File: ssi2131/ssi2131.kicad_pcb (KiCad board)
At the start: 2 copper layers, 40.2 x 108 mm, 34 parts, among them J1 Saw Out, J2 Pulse Out, J3 Tri Out, J4 Hard Sync, J5 Soft Sync, J6 Expo Freq, J7 16-Pin uZeus Power Header, U1 SSI2131, U2 LM4040DBZ-2.5

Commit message: PCB attempt 1
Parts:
- removed J6: Expo Freq, Connector_Audio:Jack_3.5mm_QingPu_WQP-PJ398SM_Vertical_CircularHoles
- added J9: Expo Freq, Connector_Audio:Jack_3.5mm_QingPu_WQP-PJ398SM_Vertical_CircularHoles, F.Cu at (135.3, 55.9)
- C1, C2, C3, C4, C5, C6, C7: footprint Capacitor_THT:C_Disc_D9.0mm_W2.5mm_P5.00mm -> Capacitor_THT:C_Disc_D6.0mm_W2.5mm_P5.00mm
- J7: footprint Connector_PinHeader_2.54mm:PinHeader_2x08_P2.54mm_Horizontal -> Connector_PinHeader_2.54mm:PinHeader_2x08_P2.54mm_Vertical; moved to B.Cu
- R1, R10, R13, R16, R2, R3, R4, R5, R6, R7, R9: footprint Resistor_THT:R_Axial_DIN0207_L6.3mm_D2.5mm_P10.16mm_Horizontal -> Resistor_THT:R_Axial_DIN0207_L6.3mm_D2.5mm_P2.54mm_Vertical
- R11: value 100 kOhms -> 220 kOhms; footprint Resistor_THT:R_Axial_DIN0207_L6.3mm_D2.5mm_P10.16mm_Horizontal -> Resistor_THT:R_Axial_DIN0207_L6.3mm_D2.5mm_P2.54mm_Vertical
- R12: value 100 kOhms -> 47 kOhms; footprint Resistor_THT:R_Axial_DIN0207_L6.3mm_D2.5mm_P10.16mm_Horizontal -> Resistor_THT:R_Axial_DIN0207_L6.3mm_D2.5mm_P2.54mm_Vertical
- R14: value 220 kOhms -> 100 kOhms; footprint Resistor_THT:R_Axial_DIN0207_L6.3mm_D2.5mm_P10.16mm_Horizontal -> Resistor_THT:R_Axial_DIN0207_L6.3mm_D2.5mm_P2.54mm_Vertical
- R15: value 47 kOhms -> 100 kOhms; footprint Resistor_THT:R_Axial_DIN0207_L6.3mm_D2.5mm_P10.16mm_Horizontal -> Resistor_THT:R_Axial_DIN0207_L6.3mm_D2.5mm_P2.54mm_Vertical
- RV2: value Expo Scale Knob - 5 kOhms -> Expo Scale Trim - 5 kOhms; moved to B.Cu
- moved C1 138.3 mm to (112.9, 38.1)
- moved C6 123.0 mm to (106.7, 58.4), turned to 180 degrees
- moved C2 119.8 mm to (114.3, 48.3), turned to 180 degrees
- moved C4 112.0 mm to (96.5, 81.3), turned to 180 degrees
- moved U2 111.4 mm to (94.0, 104.1), turned to -90 degrees
- moved C3 104.3 mm to (111.8, 121.9), turned to 90 degrees
- moved C7 97.4 mm to (116.8, 76.2), turned to 180 degrees
- moved C5 92.2 mm to (116.8, 81.3), turned to 180 degrees
- moved R8 89.1 mm to (101.6, 109.2), turned to 90 degrees
- moved R10 84.1 mm to (101.6, 94.0)
- moved U1 83.9 mm to (114.3, 94.0), turned to 180 degrees
- moved R1 82.0 mm to (94.0, 86.4)
- moved R4 81.9 mm to (123.1, 38.1), turned to 180 degrees
- moved R3 80.5 mm to (94.0, 96.5)
- moved R2 77.1 mm to (94.0, 91.4)
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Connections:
- net +2V5 renamed VREF
- net Net-(C1-Pad2) renamed HardSync
- net Net-(C2-Pad1) renamed SoftSync
- net Net-(C5-Pad1) renamed TCAP
- net Net-(J1-PadT) renamed SawOut
- net Net-(J2-PadT) renamed PulseOut
- net Net-(J3-PadT) renamed TriOut
- net Net-(R10-Pad2) renamed LinFreq
- net Net-(R5-Pad1) renamed BWComp
- net Net-(RV1-Pad2) renamed PWMCtrl
- net Net-(RV2-Pad1) renamed ExpoScale
- J7 pad 11: unconnected-(J7-Pad11) -> +5V
- J7 pad 12: unconnected-(J7-Pad12) -> +5V
- J7 pad 2: unconnected-(J7-Pad2) -> -12V
- J7 pad 4: unconnected-(J7-Pad4) -> GND
- J7 pad 6: unconnected-(J7-Pad6) -> GND
- J7 pad 8: unconnected-(J7-Pad8) -> GND
- J7 pad 9: +5V -> unconnected-(J7-Pad9)
- R11 pad 1: Net-(J6-PadT) -> Net-(R11-Pad1)
- R11 pad 2: Net-(R11-Pad2) -> ExpoFreq
- R12 pad 1: Net-(J6-PadT) -> HFTrack
- R12 pad 2: Net-(R11-Pad2) -> Net-(R11-Pad1)
- R14 pad 1: Net-(R11-Pad2) -> Net-(J9-PadT)
- R14 pad 2: Net-(R14-Pad2) -> ExpoFreq
- R15 pad 1: Net-(R14-Pad2) -> Net-(J9-PadT)
- R15 pad 2: Net-(R15-Pad2) -> ExpoFreq
- R6 pad 1: Net-(R15-Pad2) -> HFTrack
- R7 pad 1: Net-(R15-Pad2) -> HFTrack
- U1 pad 5: Net-(R15-Pad2) -> HFTrack
- U1 pad 6: Net-(R11-Pad2) -> ExpoFreq
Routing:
- net VREF: track 0.00 -> 193.2 mm
- net -12V: track 0.00 -> 112.5 mm
- net +5V: track 0.00 -> 68.6 mm
- net HardSync: track 0.00 -> 64.0 mm
- net SoftSync: track 0.00 -> 55.3 mm
- net ExpoFreq: track 0.00 -> 50.7 mm
- net HFTrack: track 0.00 -> 36.0 mm
- net ExpoScale: track 0.00 -> 34.8 mm
- net SawOut: track 0.00 -> 23.9 mm
- net Net-(R13-Pad1): track 0.00 -> 21.4 mm
- net PWMCtrl: track 0.00 -> 19.3 mm
- net TCAP: track 0.00 -> 16.9 mm
- net LinFreq: track 0.00 -> 16.6 mm
- net TriOut: track 0.00 -> 16.5 mm
- net PulseOut: track 0.00 -> 12.7 mm
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- added copper zone on B.Cu, net GND
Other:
- board size 40.2 x 108 mm -> 50.4 x 108 mm

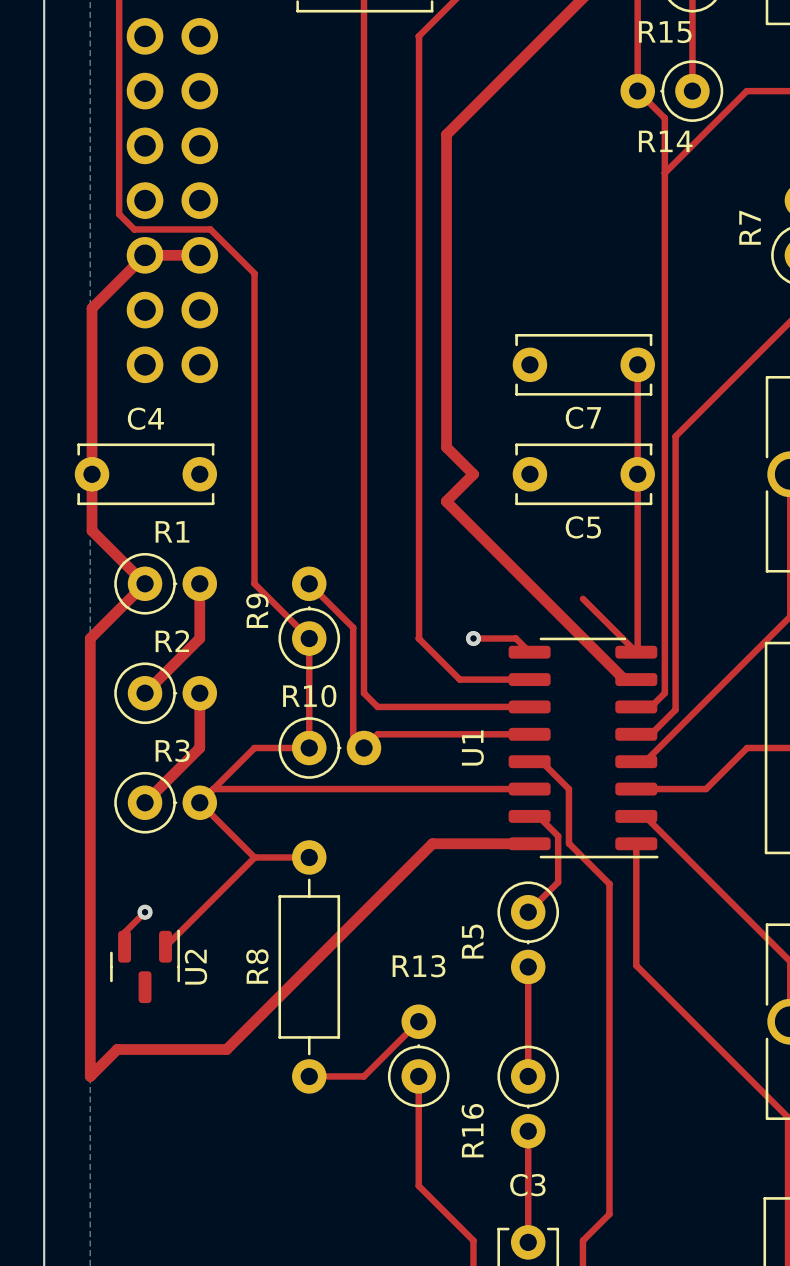
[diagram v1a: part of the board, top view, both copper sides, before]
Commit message: Add revision info, adjust tracks and spacing
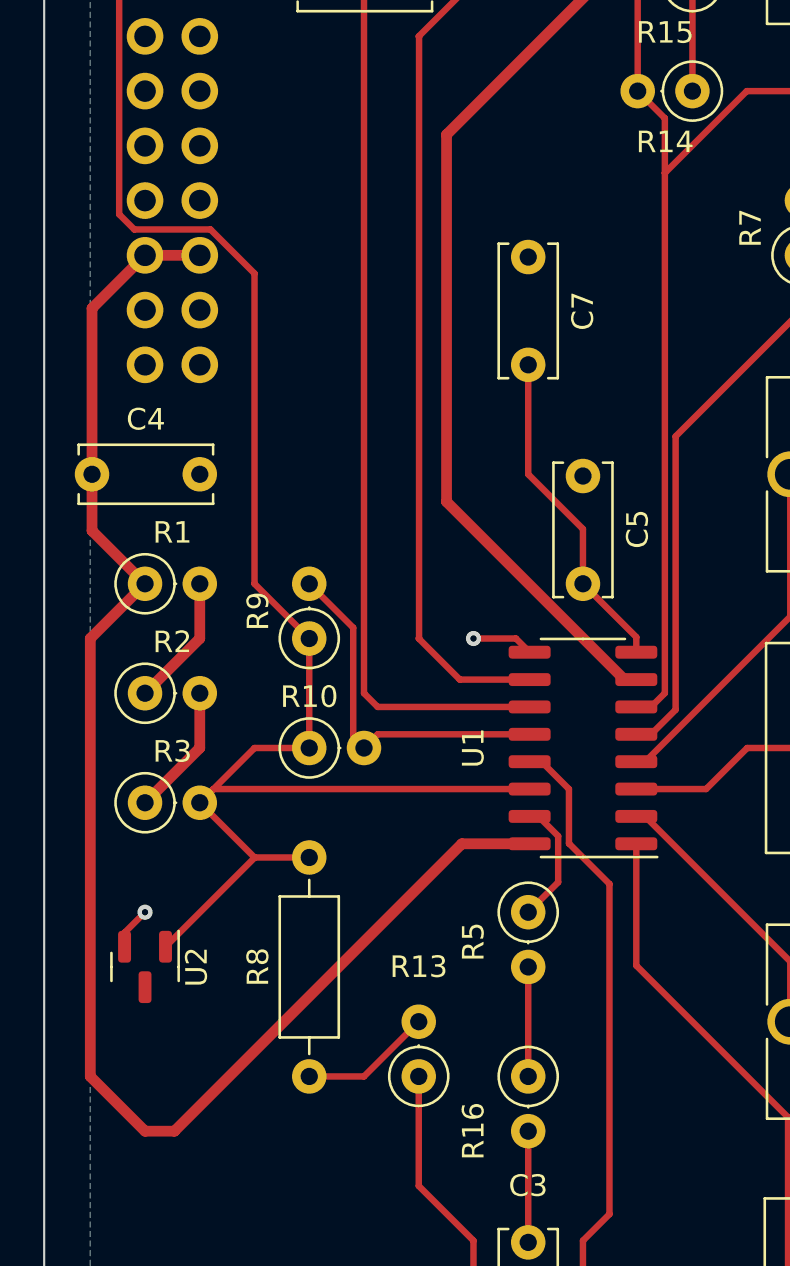
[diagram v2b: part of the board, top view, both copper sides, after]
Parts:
- moved C5 5.68 mm to (114.3, 86.4), turned to 90 degrees
- moved C7 5.08 mm to (111.8, 76.2), turned to 90 degrees
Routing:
- net +5V: track 68.6 -> 70.7 mm
- net TCAP: track 16.9 -> 15.4 mm
- net -12V: track 112.5 -> 111.5 mm
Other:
- board text added: "SSI2131 Typical Application Circuit Revision 1 9/30/2022"
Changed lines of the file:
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@@
   (net 32 "unconnected-(J7-Pad10)")
   (footprint "Capacitor_THT:C_Disc_D6.0mm_W2.5mm_P5.00mm" (layer "F.Cu")
-    (at 116.84 81.28 180)
+    (at 114.3 86.36 90)
     (descr "C, Disc series, Radial, pin pitch=5.00mm, , diameter*width=6*2.5mm^2, Capacitor, http://cdn-reichelt.de/documents/datenblatt/B300/DS_KERKO_TC.pdf")
     (tags "C Disc series Radial pin pitch 5.00mm  diameter 6mm width 2.5mm Capacitor")
@@
     (property "Sheetname" "")
     (attr through_hole)
-    (fp_text reference "C5" (at 2.5 -2.5) (layer "F.SilkS")
-      (effects (font (size 1 1) (thickness 0.15)))
-    )
-    (fp_text value "3.3 nF" (at 2.5 2.5) (layer "F.Fab")
-      (effects (font (size 1 1) (thickness 0.15)))
-    )
-    (fp_text user "${REFERENCE}" (at 2.5 0) (layer "F.Fab")
+    (fp_text reference "C5" (at 2.54 2.54 90) (layer "F.SilkS")
+      (effects (font (size 1 1) (thickness 0.15)))
+    )
+    (fp_text value "3.3 nF" (at 2.5 2.5 90) (layer "F.Fab")
+      (effects (font (size 1 1) (thickness 0.15)))
+    )
+    (fp_text user "${REFERENCE}" (at 2.5 0 90) (layer "F.Fab")
       (effects (font (size 1 1) (thickness 0.15)))
     )
@@
     (fp_line (start -0.5 1.25) (end 5.5 1.25) (layer "F.Fab") (width 0.1))
     (fp_line (start 5.5 1.25) (end 5.5 -1.25) (layer "F.Fab") (width 0.1))
-    (pad "1" thru_hole circle (at 0 0 180) (size 1.6 1.6) (drill 0.8) (layers *.Cu *.Mask)
+    (pad "1" thru_hole circle (at 0 0 90) (size 1.6 1.6) (drill 0.8) (layers *.Cu *.Mask)
       (net 8 "TCAP") (pintype "passive"))
-    (pad "2" thru_hole circle (at 5 0 180) (size 1.6 1.6) (drill 0.8) (layers *.Cu *.Mask)
+    (pad "2" thru_hole circle (at 5 0 90) (size 1.6 1.6) (drill 0.8) (layers *.Cu *.Mask)
       (net 5 "GND") (pintype "passive"))
     (model "${KICAD6_3DMODEL_DIR}/Capacitor_THT.3dshapes/C_Disc_D6.0mm_W2.5mm_P5.00mm.wrl"
@@
   )
   (footprint "Capacitor_THT:C_Disc_D6.0mm_W2.5mm_P5.00mm" (layer "F.Cu")
-    (at 116.84 76.2 180)
+    (at 111.76 76.2 90)
     (descr "C, Disc series, Radial, pin pitch=5.00mm, , diameter*width=6*2.5mm^2, Capacitor, http://cdn-reichelt.de/documents/datenblatt/B300/DS_KERKO_TC.pdf")
     (tags "C Disc series Radial pin pitch 5.00mm  diameter 6mm width 2.5mm Capacitor")
@@
     (property "Sheetname" "")
     (attr through_hole)
-    (fp_text reference "C7" (at 2.5 -2.5) (layer "F.SilkS")
-      (effects (font (size 1 1) (thickness 0.15)))
-    )
-    (fp_text value "680 pF" (at 2.5 2.5) (layer "F.Fab")
-      (effects (font (size 1 1) (thickness 0.15)))
-    )
-    (fp_text user "${REFERENCE}" (at 2.5 0) (layer "F.Fab")
+    (fp_text reference "C7" (at 2.5 2.54 90) (layer "F.SilkS")
+      (effects (font (size 1 1) (thickness 0.15)))
+    )
+    (fp_text value "680 pF" (at 2.5 2.5 90) (layer "F.Fab")
+      (effects (font (size 1 1) (thickness 0.15)))
+    )
+    (fp_text user "${REFERENCE}" (at 2.5 0 90) (layer "F.Fab")
       (effects (font (size 1 1) (thickness 0.15)))
     )
@@
     (fp_line (start 5.5 -1.25) (end -0.5 -1.25) (layer "F.Fab") (width 0.1))
     (fp_line (start -0.5 1.25) (end 5.5 1.25) (layer "F.Fab") (width 0.1))
-    (pad "1" thru_hole circle (at 0 0 180) (size 1.6 1.6) (drill 0.8) (layers *.Cu *.Mask)
+    (pad "1" thru_hole circle (at 0 0 90) (size 1.6 1.6) (drill 0.8) (layers *.Cu *.Mask)
       (net 8 "TCAP") (pintype "passive"))
-    (pad "2" thru_hole circle (at 5 0 180) (size 1.6 1.6) (drill 0.8) (layers *.Cu *.Mask)
+    (pad "2" thru_hole circle (at 5 0 90) (size 1.6 1.6) (drill 0.8) (layers *.Cu *.Mask)
       (net 5 "GND") (pintype "passive"))
     (model "${KICAD6_3DMODEL_DIR}/Capacitor_THT.3dshapes/C_Disc_D6.0mm_W2.5mm_P5.00mm.wrl"
@@
   )
   (gr_rect (start 89.3 30.48) (end 139.7 138.48) (layer "Edge.Cuts") (width 0.1) (fill none))
+  (gr_text "SSI2131 Typical\nApplication Circuit\nRevision 1\n9/30/2022" (at 101.6 119.38) (layer "B.SilkS")
+    (effects (font (size 1 1) (thickness 0.15)) (justify mirror))
+  )
   (segment (start 112.91 38.1) (end 104.68 38.1) (width 0.3) (layer "F.Cu") (net 1))
   (segment (start 106.695 88.885) (end 106.68 88.9) (width 0.3) (layer "F.Cu") (net 2))
@@
   (via (at 93.98 101.6) (size 0.7) (drill 0.3) (layers "F.Cu" "B.Cu") (net 5))
   (segment (start 111.76 111.76) (end 111.76 116.92) (width 0.3) (layer "F.Cu") (net 6))
+  (segment (start 93.98 86.36) (end 91.44 88.9) (width 0.5) (layer "F.Cu") (net 7))
+  (segment (start 91.44 109.22) (end 93.98 111.76) (width 0.5) (layer "F.Cu") (net 7))
+  (segment (start 91.44 88.9) (end 91.44 109.22) (width 0.5) (layer "F.Cu") (net 7))
   (segment (start 91.52 81.28) (end 91.52 83.9) (width 0.5) (layer "F.Cu") (net 7))
+  (segment (start 108.68 98.425) (end 111.825 98.425) (width 0.5) (layer "F.Cu") (net 7))
   (segment (start 91.52 83.9) (end 93.98 86.36) (width 0.5) (layer "F.Cu") (net 7))
-  (segment (start 91.44 88.9) (end 91.44 109.22) (width 0.5) (layer "F.Cu") (net 7))
-  (segment (start 92.69 107.97) (end 97.77 107.97) (width 0.5) (layer "F.Cu") (net 7))
-  (segment (start 107.315 98.425) (end 111.825 98.425) (width 0.5) (layer "F.Cu") (net 7))
+  (segment (start 95.345 111.76) (end 108.68 98.425) (width 0.5) (layer "F.Cu") (net 7))
   (segment (start 93.98 71.12) (end 91.52 73.58) (width 0.5) (layer "F.Cu") (net 7))
-  (segment (start 91.44 109.22) (end 92.69 107.97) (width 0.5) (layer "F.Cu") (net 7))
   (segment (start 91.52 73.58) (end 91.52 81.28) (width 0.5) (layer "F.Cu") (net 7))
-  (segment (start 93.98 86.36) (end 91.44 88.9) (width 0.5) (layer "F.Cu") (net 7))
-  (segment (start 97.77 107.97) (end 107.315 98.425) (width 0.5) (layer "F.Cu") (net 7))
   (segment (start 96.52 71.12) (end 93.98 71.12) (width 0.5) (layer "F.Cu") (net 7))
-  (segment (start 116.84 81.28) (end 116.84 89.47) (width 0.3) (layer "F.Cu") (net 8))
-  (segment (start 116.84 76.2) (end 116.84 81.28) (width 0.3) (layer "F.Cu") (net 8))
-  (segment (start 116.84 89.47) (end 116.775 89.535) (width 0.3) (layer "F.Cu") (net 8))
-  (segment (start 114.3 87.06) (end 116.775 89.535) (width 0.3) (layer "F.Cu") (net 8))
+  (segment (start 93.98 111.76) (end 95.345 111.76) (width 0.5) (layer "F.Cu") (net 7))
+  (segment (start 114.3 83.82) (end 114.3 86.36) (width 0.3) (layer "F.Cu") (net 8))
+  (segment (start 116.775 88.835) (end 116.775 89.535) (width 0.3) (layer "F.Cu") (net 8))
+  (segment (start 111.76 76.2) (end 111.76 81.28) (width 0.3) (layer "F.Cu") (net 8))
+  (segment (start 111.76 81.28) (end 114.3 83.82) (width 0.3) (layer "F.Cu") (net 8))
+  (segment (start 114.3 86.36) (end 116.775 88.835) (width 0.3) (layer "F.Cu") (net 8))
+  (segment (start 116.221472 90.805) (end 116.775 90.805) (width 0.5) (layer "F.Cu") (net 9))
+  (segment (start 114.85 45.942233) (end 114.85 39.392233) (width 0.5) (layer "F.Cu") (net 9))
   (segment (start 121.78 51.712233) (end 107.97 65.522233) (width 0.5) (layer "F.Cu") (net 9))
-  (segment (start 109.22 81.28) (end 107.97 82.53) (width 0.5) (layer "F.Cu") (net 9))
-  (segment (start 116.221472 90.805) (end 116.775 90.805) (width 0.5) (layer "F.Cu") (net 9))
+  (segment (start 121.047767 36.85) (end 121.78 37.582233) (width 0.5) (layer "F.Cu") (net 9))
+  (segment (start 93.98 58.42) (end 96.52 58.42) (width 0.5) (layer "F.Cu") (net 9))
+  (segment (start 102.372233 58.42) (end 114.85 45.942233) (width 0.5) (layer "F.Cu") (net 9))
+  (segment (start 107.97 65.522233) (end 107.97 82.553528) (width 0.5) (layer "F.Cu") (net 9))
+  (segment (start 93.98 58.42) (end 102.372233 58.42) (width 0.5) (layer "F.Cu") (net 9))
+  (segment (start 114.85 39.392233) (end 117.392233 36.85) (width 0.5) (layer "F.Cu") (net 9))
   (segment (start 107.97 82.553528) (end 116.221472 90.805) (width 0.5) (layer "F.Cu") (net 9))
-  (segment (start 107.97 82.53) (end 107.97 82.553528) (width 0.5) (layer "F.Cu") (net 9))
+  (segment (start 121.78 37.582233) (end 121.78 51.712233) (width 0.5) (layer "F.Cu") (net 9))
   (segment (start 117.392233 36.85) (end 121.047767 36.85) (width 0.5) (layer "F.Cu") (net 9))
-  (segment (start 107.97 65.522233) (end 107.97 80.03) (width 0.5) (layer "F.Cu") (net 9))
-  (segment (start 121.047767 36.85) (end 121.78 37.582233) (width 0.5) (layer "F.Cu") (net 9))
-  (segment (start 121.78 37.582233) (end 121.78 51.712233) (width 0.5) (layer "F.Cu") (net 9))
-  (segment (start 93.98 58.42) (end 96.52 58.42) (width 0.5) (layer "F.Cu") (net 9))
-  (segment (start 114.85 45.942233) (end 114.85 39.392233) (width 0.5) (layer "F.Cu") (net 9))
-  (segment (start 107.97 80.03) (end 109.22 81.28) (width 0.5) (layer "F.Cu") (net 9))
-  (segment (start 114.85 39.392233) (end 117.392233 36.85) (width 0.5) (layer "F.Cu") (net 9))
-  (segment (start 102.372233 58.42) (end 114.85 45.942233) (width 0.5) (layer "F.Cu") (net 9))
-  (segment (start 93.98 58.42) (end 102.372233 58.42) (width 0.5) (layer "F.Cu") (net 9))
   (segment (start 101.68 58.42) (end 96.52 58.42) (width 0.5) (layer "F.Cu") (net 9))
   (segment (start 96.52 86.36) (end 96.52 88.9) (width 0.5) (layer "F.Cu") (net 10))

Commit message: rework PCB layout
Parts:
- removed C7: 680 pF, Capacitor_THT:C_Disc_D6.0mm_W2.5mm_P5.00mm
- removed R10: 1 MOhms, Resistor_THT:R_Axial_DIN0207_L6.3mm_D2.5mm_P2.54mm_Vertical
- removed R12, R7: 47 kOhms, Resistor_THT:R_Axial_DIN0207_L6.3mm_D2.5mm_P2.54mm_Vertical
- removed R13: 100 Ohms, Resistor_THT:R_Axial_DIN0207_L6.3mm_D2.5mm_P2.54mm_Vertical
- removed R15: 100 kOhms, Resistor_THT:R_Axial_DIN0207_L6.3mm_D2.5mm_P2.54mm_Vertical
- removed R16: 47 Ohms, Resistor_THT:R_Axial_DIN0207_L6.3mm_D2.5mm_P2.54mm_Vertical
- removed R2: 2.2 kOhms, Resistor_THT:R_Axial_DIN0207_L6.3mm_D2.5mm_P2.54mm_Vertical
- removed R3: 1 kOhms, Resistor_THT:R_Axial_DIN0207_L6.3mm_D2.5mm_P2.54mm_Vertical
- C5: value 3.3 nF -> 3.9 nF
- R1: value 4.7 kOhms -> 7.5 kOhms
- R11: value 220 kOhms -> 267 kOhms
- R14: value 100 kOhms -> 49.9 kOhms
- R5: value 220 Ohms -> 267 Ohms
- R6: value 4.7 kOhms -> 4.3 kOhms
- R8: value 22 kOhms -> 22.1 kOhms
- R9: value 1 MOhms -> 499 kOhms; footprint Resistor_THT:R_Axial_DIN0207_L6.3mm_D2.5mm_P2.54mm_Vertical -> Resistor_THT:R_Axial_DIN0207_L6.3mm_D2.5mm_P10.16mm_Horizontal
- moved J4 108.8 mm to (172.7, 112.5), turned to 180 degrees
- moved R8 96.6 mm to (188.0, 66.0), turned to 180 degrees
- moved J5 94.5 mm to (162.6, 112.5), turned to 180 degrees
- moved RV2 93.4 mm to (180.3, 61.0), turned to 180 degrees
- moved U2 82.4 mm to (168.9, 69.8), turned to 0 degrees
- moved C6 82.2 mm to (187.9, 71.1), turned to -90 degrees
- moved C1 78.3 mm to (165.1, 96.5)
- moved R9 77.9 mm to (175.3, 63.5), turned to -90 degrees
- moved R4 76.7 mm to (172.7, 96.5), turned to 90 degrees
- moved C4 76.4 mm to (167.6, 53.3), turned to 90 degrees
- moved J9 73.9 mm to (182.9, 112.5), turned to 180 degrees
- moved C3 73.6 mm to (173.9, 82.5), turned to 180 degrees
- moved J3 72.0 mm to (182.9, 135.3), turned to 180 degrees
- moved R14 71.1 mm to (181.6, 97.8), turned to 90 degrees
- moved C5 70.8 mm to (184.2, 74.9), turned to 180 degrees
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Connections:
- C3 pad 2: Net-(C3-Pad2) -> Net-(R5-Pad2)
- R1 pad 2: Net-(R1-Pad2) -> VREF
- R11 pad 1: Net-(R11-Pad1) -> HFTrack
- R5 pad 2: Net-(R16-Pad1) -> Net-(R5-Pad2)
- R8 pad 1: Net-(R13-Pad2) -> Net-(R8-Pad1)
- RV2 pad 2: Net-(R13-Pad1) -> Net-(R8-Pad1)
- RV2 pad 3: Net-(R13-Pad1) -> Net-(R8-Pad1)
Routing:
- net VREF: track 193.2 -> 35.3 mm
- net -12V: track 111.5 -> 68.8 mm, vias 0 -> 2
- net HardSync: track 64.0 -> 23.5 mm
- net TriOut: track 16.5 -> 51.8 mm
- net PulseOut: track 12.7 -> 46.8 mm
- net ExpoFreq: track 50.7 -> 23.2 mm
- net SawOut: track 23.9 -> 49.9 mm
- net SoftSync: track 55.3 -> 29.5 mm
- net Net-(R13-Pad1): track 21.4 -> 0.00 mm
- net HFTrack: track 36.0 -> 16.8 mm
- net TCAP: track 15.4 -> 2.46 mm
- net PWMCtrl: track 19.3 -> 30.6 mm
- net +5V: track 70.7 -> 60.6 mm
- net ExpoScale: track 34.8 -> 25.5 mm
- net Net-(R8-Pad1): track 0.00 -> 8.67 mm
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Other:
- board text added: "SSI2131 Typical Application Circuit Revision 2 9/30/2022"
- board text removed: "SSI2131 Typical Application Circuit Revision 1 9/30/2022"
